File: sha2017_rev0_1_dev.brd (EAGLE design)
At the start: 65 x 80 mm, 87 parts, among them IC1 AP7215, IC2 LM1117, IC3 CP210X_USB_UART, IC5 ESP32WROOM32, Q1 MMBT2222A, Q2 MMBT2222A, Q3 SI1304 BDL, SW100 MCMT5-F-V, X701 2908-05WB-MG

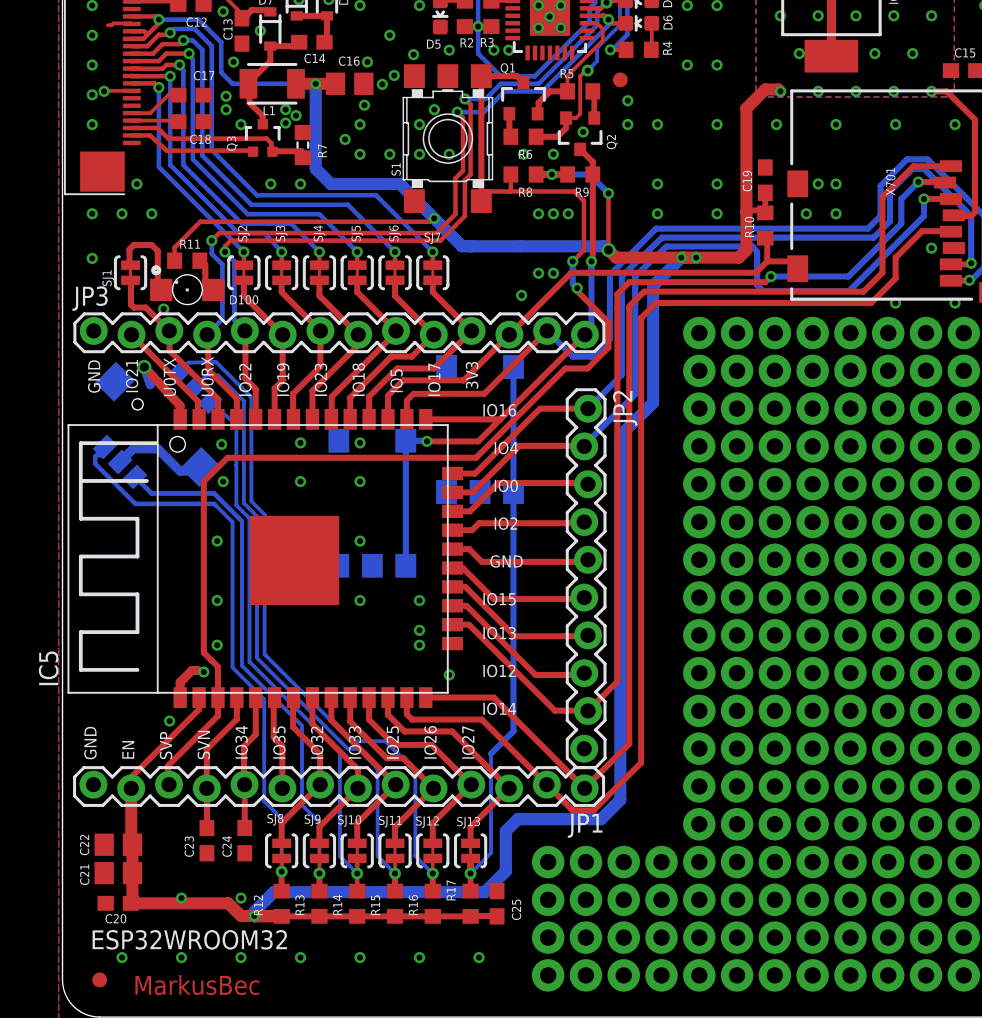
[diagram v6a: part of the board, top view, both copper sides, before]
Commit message: fixed silkscreen
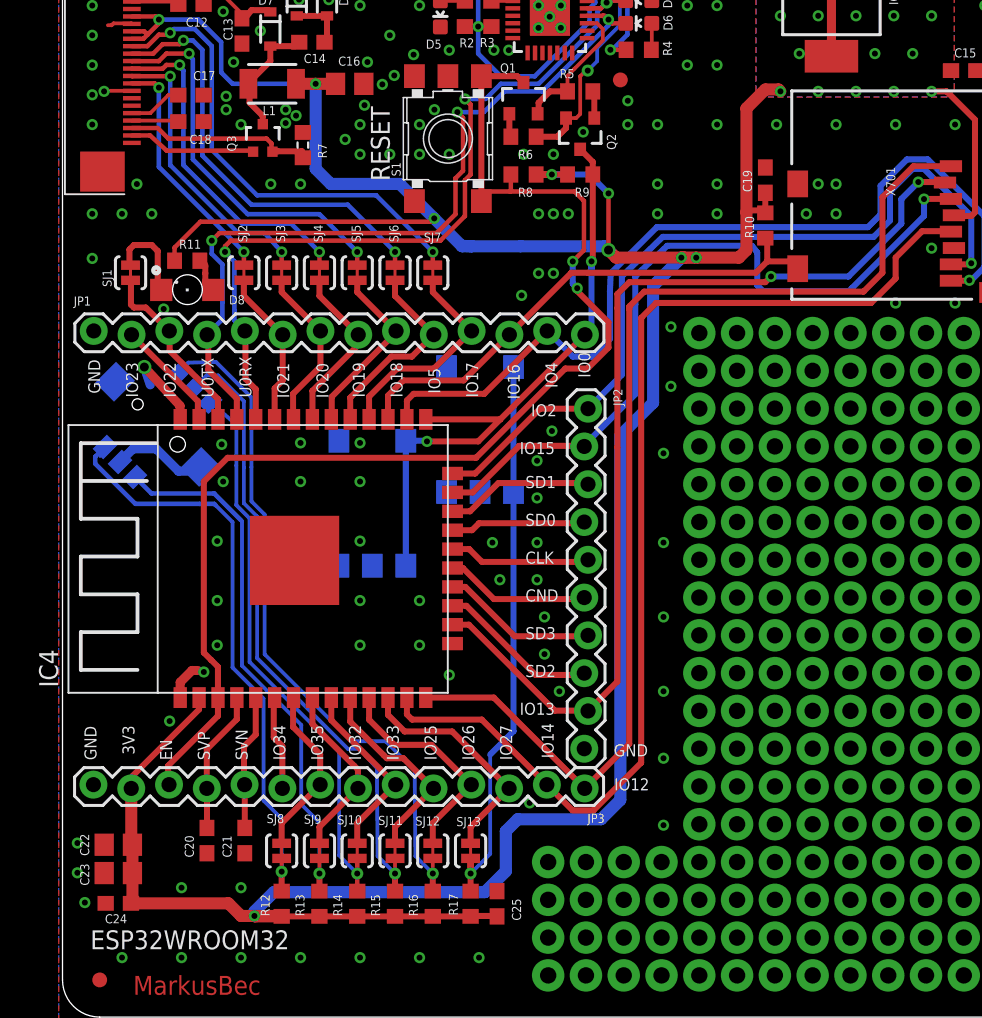
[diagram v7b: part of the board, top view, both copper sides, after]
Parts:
- C20: value 100n -> (none)
- C21: value 4u7/16V -> (none); device rcl:C0805 -> rcl:C0603
- C23: value (none) -> 4u7/16V; device rcl:C0603 -> rcl:C0805
- C24: value (none) -> 100n
- moved FD5 75.7 mm to (2.50, 2.50)
- moved FD1 75.0 mm to (2.50, 77.5)
- moved FD2 60.0 mm to (62.5, 77.5)
- moved JP1 44.9 mm to (2.10, 46.0), turned to 0 degrees
- moved JP3 44.9 mm to (35.1, 15.5), turned to 180 degrees
- moved FD3 35.2 mm to (27.5, 74.0)
- moved C24 9.49 mm to (3.75, 7.65), turned to 180 degrees
- moved C21 8.78 mm to (12.3, 11.9), turned to 90 degrees
- moved C20 7.30 mm to (9.71, 11.9), turned to 90 degrees
- moved C23 6.35 mm to (3.75, 9.68), turned to 180 degrees
- renumbered D100 to D8, IC5 to IC4
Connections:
- net +3V3: now also C23.1, C24.1, JP3.13; no longer C20.1, C21.1, JP1.13
- net ESP32_!RESET: now also JP3.12; no longer JP1.12
- net ESP32_FLASH/TOUCHE_MENU: now also JP1.14; no longer JP3.14
- net ESP32_RX: now also JP1.5; no longer JP3.5
- net ESP32_TX: now also JP1.4; no longer JP3.4
- net GND: now also C20.1, C21.1, C23.2, C24.2, JP1.1, JP3.14; no longer C20.2, C21.2, C23.1, C24.1, JP1.14, JP3.1
- net N$1: now also JP3.9; no longer JP1.9
- net N$15: now also JP1.2; no longer JP3.2
- net N$16: now also JP1.3; no longer JP3.3
- net N$17: now also JP1.6; no longer JP3.6
- net N$18: now also JP1.7; no longer JP3.7
- net N$20: now also JP1.9; no longer JP3.9
- net N$21: now also JP1.10; no longer JP3.10
- net N$24: now also JP1.11; no longer JP3.11
- net N$42: now also C20.2, JP3.11; no longer C23.2, JP1.11
- net N$43: now also C21.2, JP3.10; no longer C24.2, JP1.10
- net N$44: now also JP3.8; no longer JP1.8
- net N$45: now also JP3.7; no longer JP1.7
- net N$46: now also JP3.6; no longer JP1.6
- net N$47: now also JP3.5; no longer JP1.5
- net N$48: now also JP3.4; no longer JP1.4
- net N$49: now also JP3.3; no longer JP1.3
- net N$63: now also JP1.8; no longer JP3.8
- net SD_CD: now also JP1.12; no longer JP3.12
- net SD_CLK: now also JP3.2; no longer JP1.2
- net SD_DATA1: now also JP1.13; no longer JP3.13
- net SD_DATA2: now also JP3.1; no longer JP1.1
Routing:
- net GND: vias 149 -> 171
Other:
- board text added: "A"
- board text added: "B"
- board text added: "CLK"
- board text added: "CND"
- board text added: "FLASH"
- board text added: "IO20"
- board text added: "RESET"
- board text added: "SD0"
- board text added: "SD1"
- board text added: "SD2"
- board text added: "SD3"
